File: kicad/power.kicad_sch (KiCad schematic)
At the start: 26 parts, among them J13 USB4125-GF-A, K1 J1071CS5VDC.36, SW1 ANT11TFHQE, SW2 PTS645VL58-2 LFS, U40 MCP1700-3302E/TO, X1 25.175 MHz

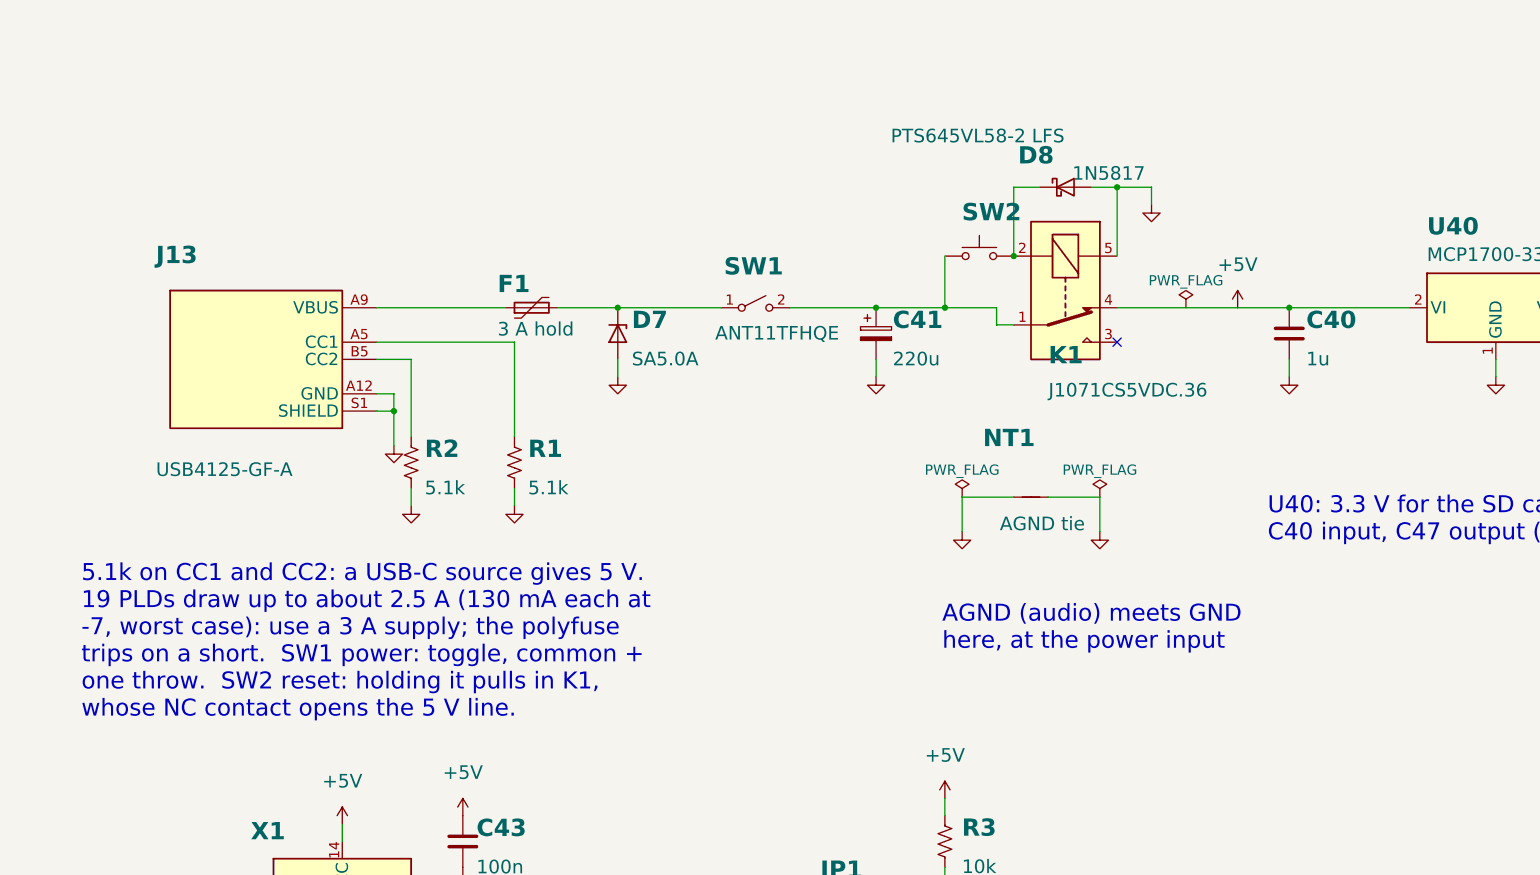
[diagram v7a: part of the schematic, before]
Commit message: Move C41 to +5V after K1 and drain the rail through K1's NO contact
K1's COM now carries +5V and its NC contact VON, so holding reset swings
COM onto the NO contact, where new R64 (22 ohm) empties the board rail in
a few ms however short the press.  C41 (220u) moves from VON to +5V so it
carries the board through the NC contact's bounce when reset lets go.
Power sheet relaid (NT1 moved down), BOMs, BRINGUP and SCHEMATIC_PLAN
updated; BRINGUP's K1 part number typo (CS6VDC) fixed.

Co-Authored-By: Claude Opus 5.5 <noreply@anthropic.com>
Claude-Session: https://claude.ai/code/session_01DnW5SRTxWuv4xnT2rLGBJ6
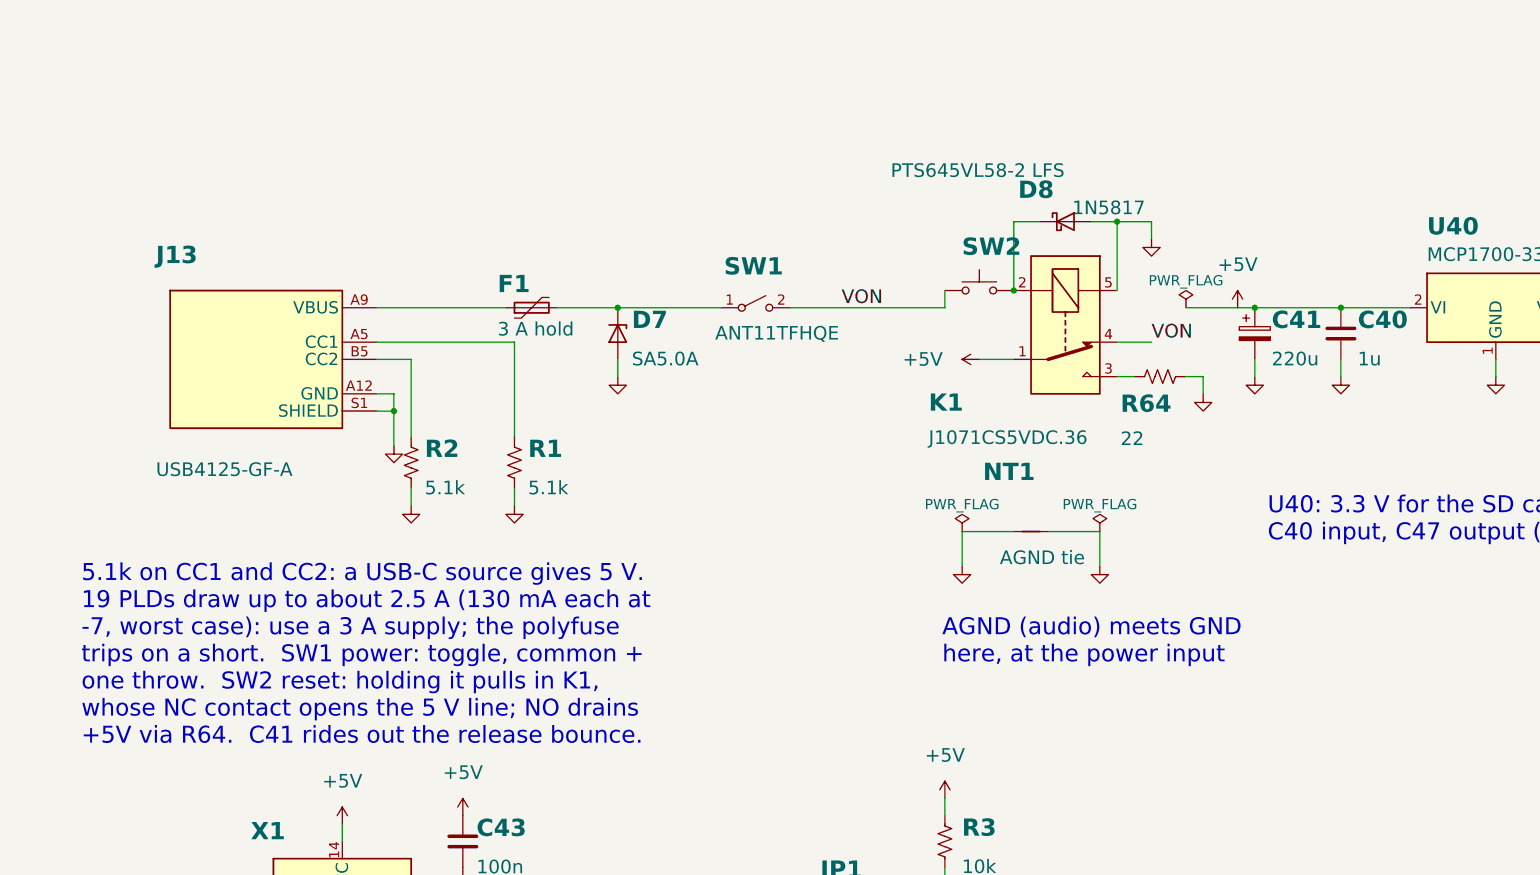
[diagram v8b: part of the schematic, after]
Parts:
- added R64: 22, placard:R_Axial_DIN0207_L6.3mm_D2.5mm_P10.16mm_Horizontal_Value, symbol placard_std:R_US
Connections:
- net +5V: now also C41.1, K1.1; no longer K1.4
- net GND: now also R64.2
- net VON: now reaches SW1.2 (B), SW2.1
- net VON: now also K1.4; no longer C41.1, K1.1
- net at K1.3: now also R64.1
- no-connect marks 1 -> 0
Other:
- note added: "+5V via R64. C41 rides out the release bounce."
- note added: "whose NC contact opens the 5 V line; NO drains"
- note removed: "whose NC contact opens the 5 V line."
- moved on the sheet: C40, C41, D8, K1, NT1, SW2
